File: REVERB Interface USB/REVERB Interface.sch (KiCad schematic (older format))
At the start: 88 parts, among them J1 RPiZeroW, J2 Iridium, J3 APRS, J4 Antenna, J6 USB_B_Micro, J7 USB, J8 USBPOGO, M1 MountingHole_Pad, M2 MountingHole_Pad, M3 MountingHole_Pad, M4 MountingHole_Pad, M5 PiMount, M6 PiMount, M7 PiMount, M8 PiMount, U1 LSM9DS1BOB, U2 MAX3232, U3 CY7C65213-28PVXI, U4 TXB0104D

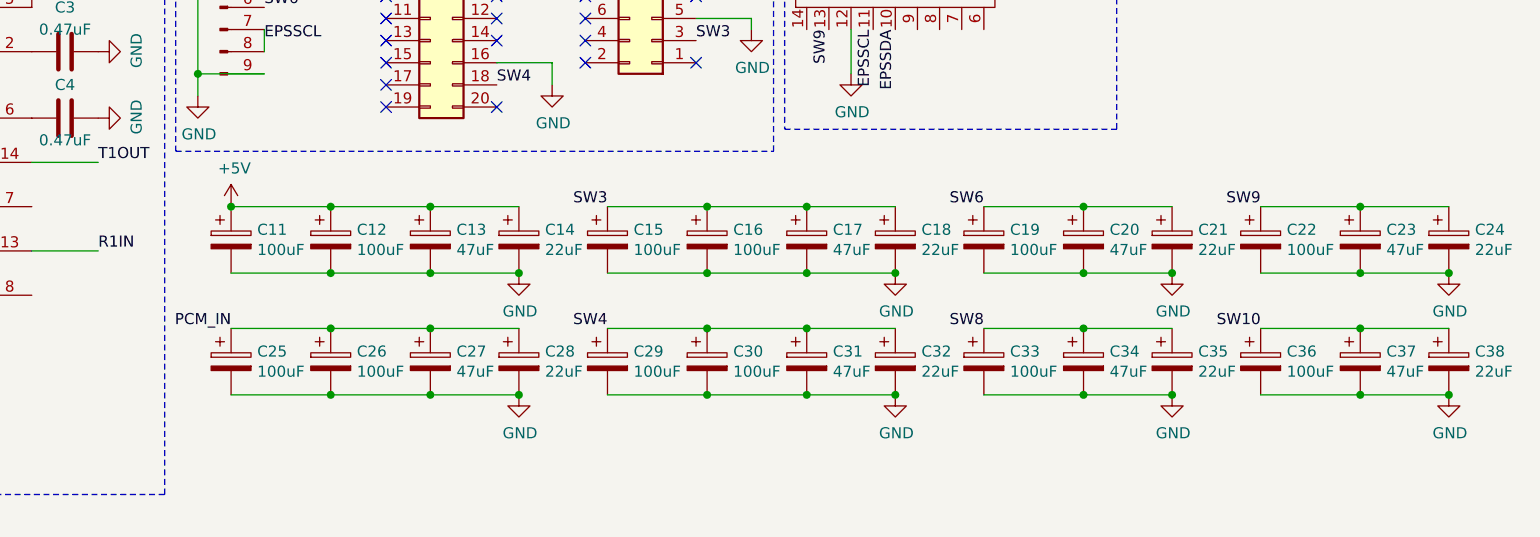
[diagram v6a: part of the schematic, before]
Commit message: Add decoupling
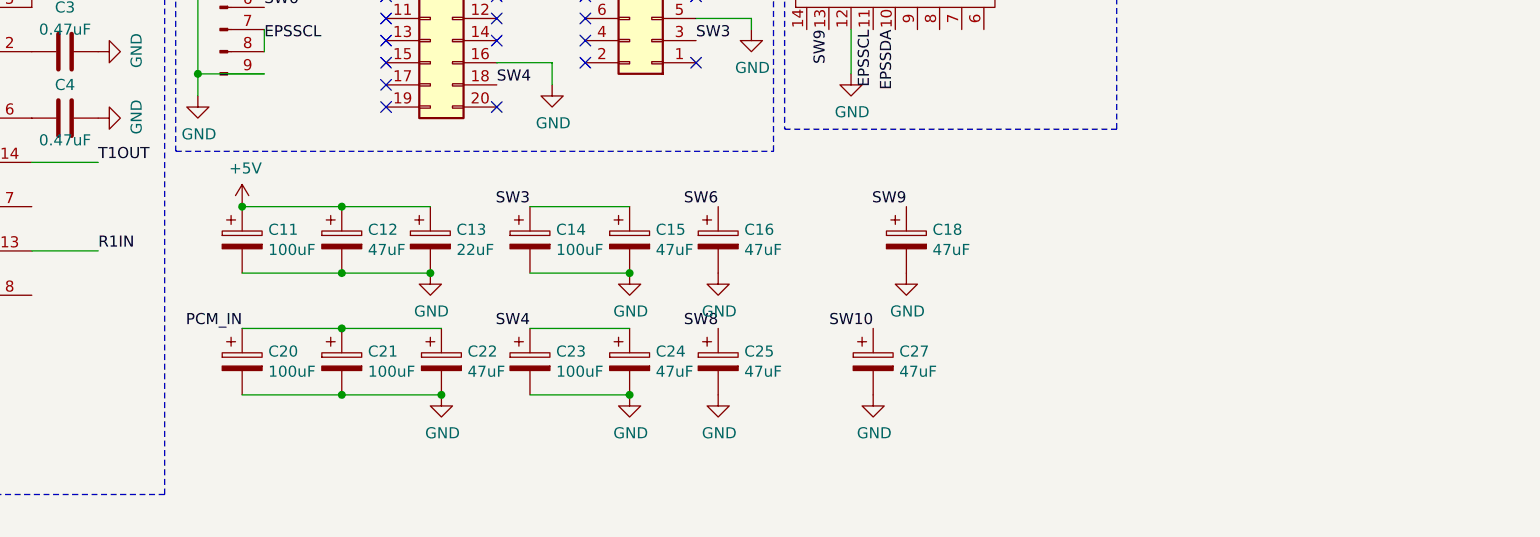
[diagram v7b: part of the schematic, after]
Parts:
- removed C17, C31, C34, C37: 47uF, Capacitor_Tantalum_SMD:CP_EIA-6032-28_Kemet-C_Pad2.25x2.35mm_HandSolder, symbol Device:CP
- removed C19, C26, C29, C30, C33, C36: 100uF, Capacitor_Tantalum_SMD:CP_EIA-7343-43_Kemet-X_Pad2.25x2.55mm_HandSolder, symbol Device:CP
- removed C28, C32, C35, C38: 22uF, Capacitor_Tantalum_SMD:CP_EIA-7343-43_Kemet-X_Pad2.25x2.55mm_HandSolder, symbol Device:CP
- C12, C15, C16, C22, C25: value 100uF -> 47uF; footprint Capacitor_Tantalum_SMD:CP_EIA-7343-43_Kemet-X_Pad2.25x2.55mm_HandSolder -> Capacitor_Tantalum_SMD:CP_EIA-6032-28_Kemet-C_Pad2.25x2.35mm_HandSolder
- C13: value 47uF -> 22uF
- C14, C21: value 22uF -> 100uF
- C18, C24: value 22uF -> 47uF; footprint Capacitor_Tantalum_SMD:CP_EIA-7343-43_Kemet-X_Pad2.25x2.55mm_HandSolder -> Capacitor_Tantalum_SMD:CP_EIA-6032-28_Kemet-C_Pad2.25x2.35mm_HandSolder
- C20, C23: value 47uF -> 100uF; footprint Capacitor_Tantalum_SMD:CP_EIA-6032-28_Kemet-C_Pad2.25x2.35mm_HandSolder -> Capacitor_Tantalum_SMD:CP_EIA-7343-43_Kemet-X_Pad2.25x2.55mm_HandSolder
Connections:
- net +5V: no longer C14.1
- net PCM_IN: now also C20.1, C21.1, C22.1; no longer C25.1, C27.1
- net SW10: now also C27.1
- net SW3: now also C14.1; no longer C16.1, C18.1
- net SW4: now also C23.1, C24.1
- net SW6: now also C16.1; no longer C20.1, C21.1
- net SW8: now also C25.1
- net SW9: now also C18.1; no longer C22.1, C23.1, C24.1

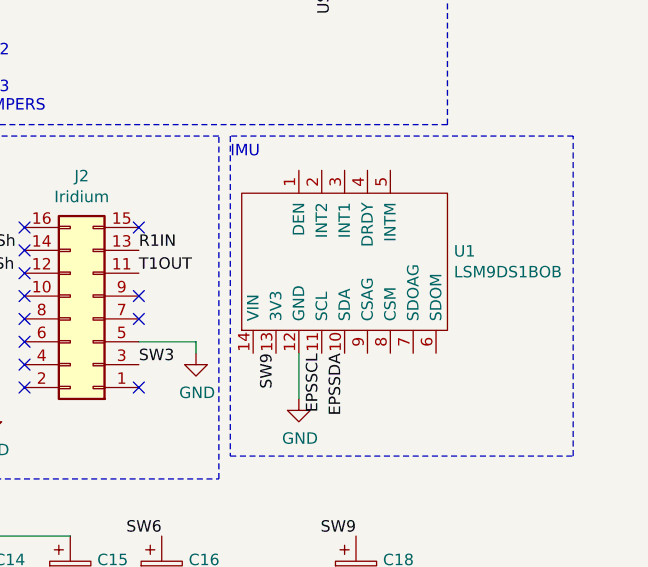
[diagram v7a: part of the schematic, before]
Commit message: fix imu implementation, add bno055 compatibility
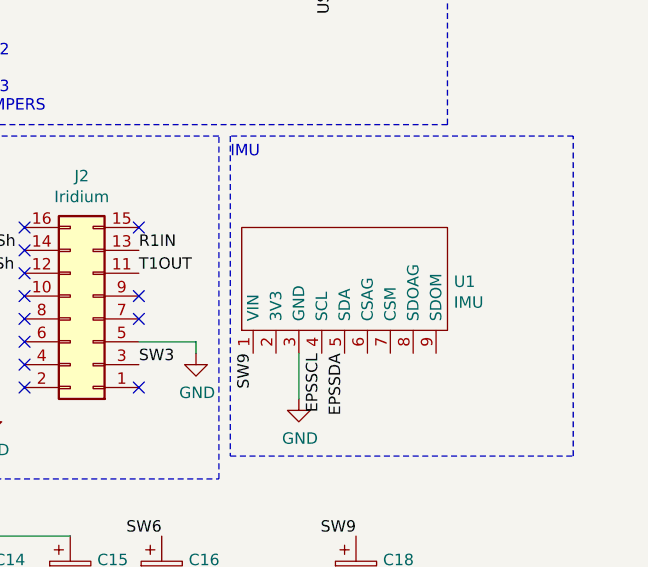
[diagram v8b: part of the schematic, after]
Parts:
- removed U1: LSM9DS1BOB, REVERB Interface:LSM9DS1BOB, symbol REVERBSym:LSM9DS1BOB
- added U1: IMU, REVERB Interface:LSM9DS1-BNO055, symbol REVERBSym:IMU
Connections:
- net EPSSCL: now also U1.4 (SCL)
- net EPSSDA: now also U1.5 (SDA)
- net GND: now also U1.3 (GND)
- net SW9: now also U1.1 (VIN)
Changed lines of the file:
@@
 Wire Notes Line
 	6600 6950 6600 3900
-$Comp
-L REVERBSym:LSM9DS1BOB U1
-U 1 1 617E2B02
-P 9900 4450
-F 0 "U1" H 10378 4496 50  0000 L CNN
-F 1 "LSM9DS1BOB" H 10378 4405 50  0000 L CNN
-F 2 "REVERB Interface:LSM9DS1BOB" H 9900 4450 50  0001 C CNN
-F 3 "" H 9900 4450 50  0001 C CNN
-	1    9900 4450
-	1    0    0    -1
-$EndComp
-Text Label 9600 4850 3    50   ~ 0
+Text Label 9500 4850 3    50   ~ 0
 SW9
 Wire Wire Line
@@
 	1    0    0    -1
 $EndComp
+$Comp
+L REVERBSym:IMU U1
+U 1 1 618A3C53
+P 9900 4450
+F 0 "U1" H 10378 4363 50  0000 L CNN
+F 1 "IMU" H 10378 4272 50  0000 L CNN
+F 2 "REVERB Interface:LSM9DS1-BNO055" H 9900 4450 50  0001 C CNN
+F 3 "" H 9900 4450 50  0001 C CNN
+	1    9900 4450
+	1    0    0    -1
+$EndComp
